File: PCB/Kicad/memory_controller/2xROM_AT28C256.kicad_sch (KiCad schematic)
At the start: 4 parts, among them U23 AT28C256-15PU, U24 AT28C256-15PU

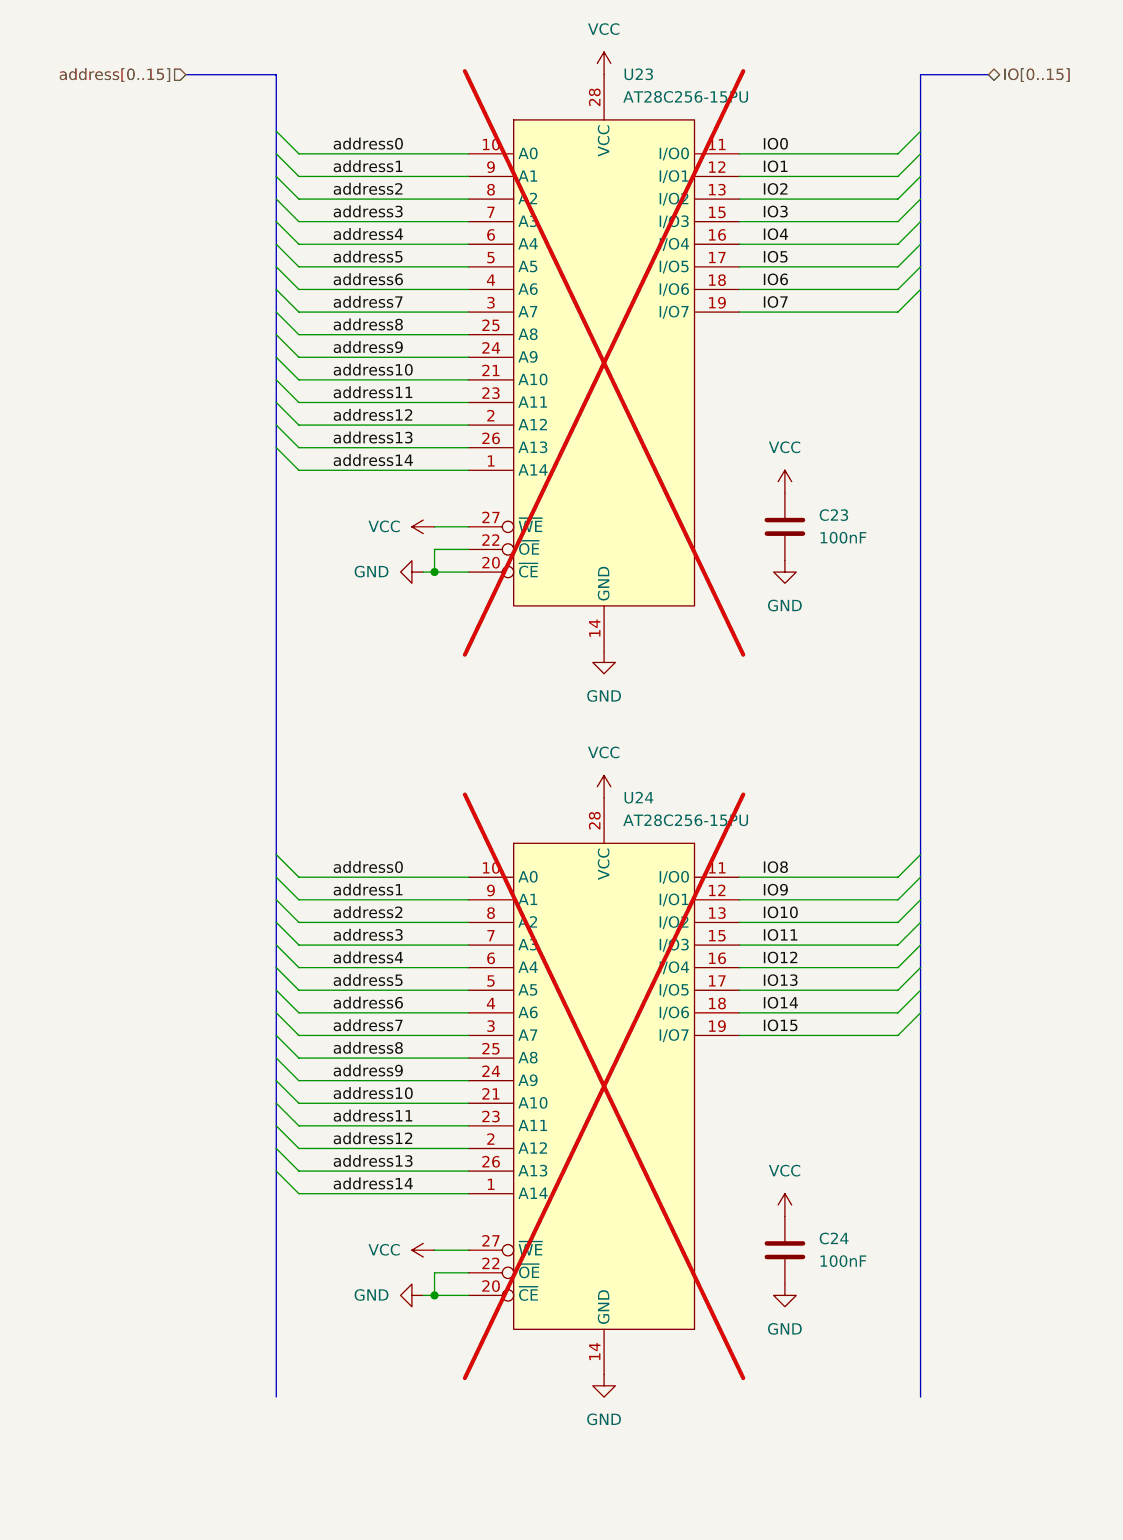
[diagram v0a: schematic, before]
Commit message: decoupling C RAM ROM
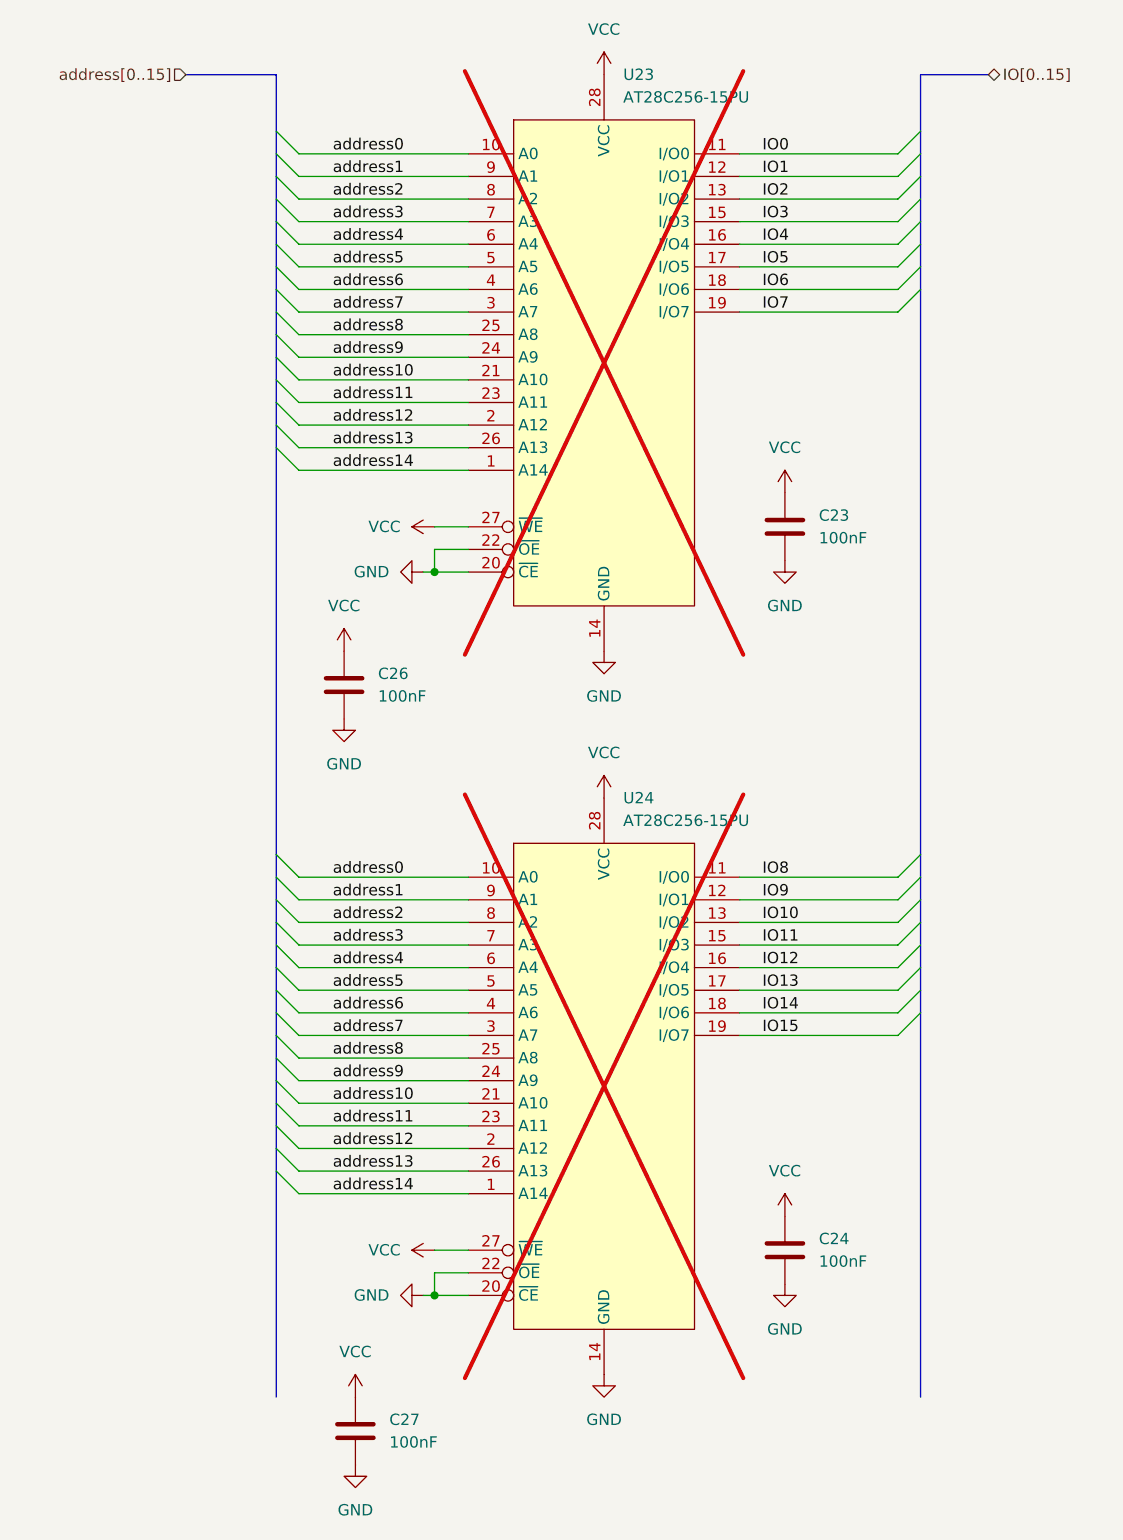
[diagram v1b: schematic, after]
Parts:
- added C26, C27: 100nF, Capacitor_SMD:C_0402_1005Metric, symbol Device:C
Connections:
- net GND: now also C26.1, C27.1
- net VCC: now also C26.2, C27.2

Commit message: board size + ground vias
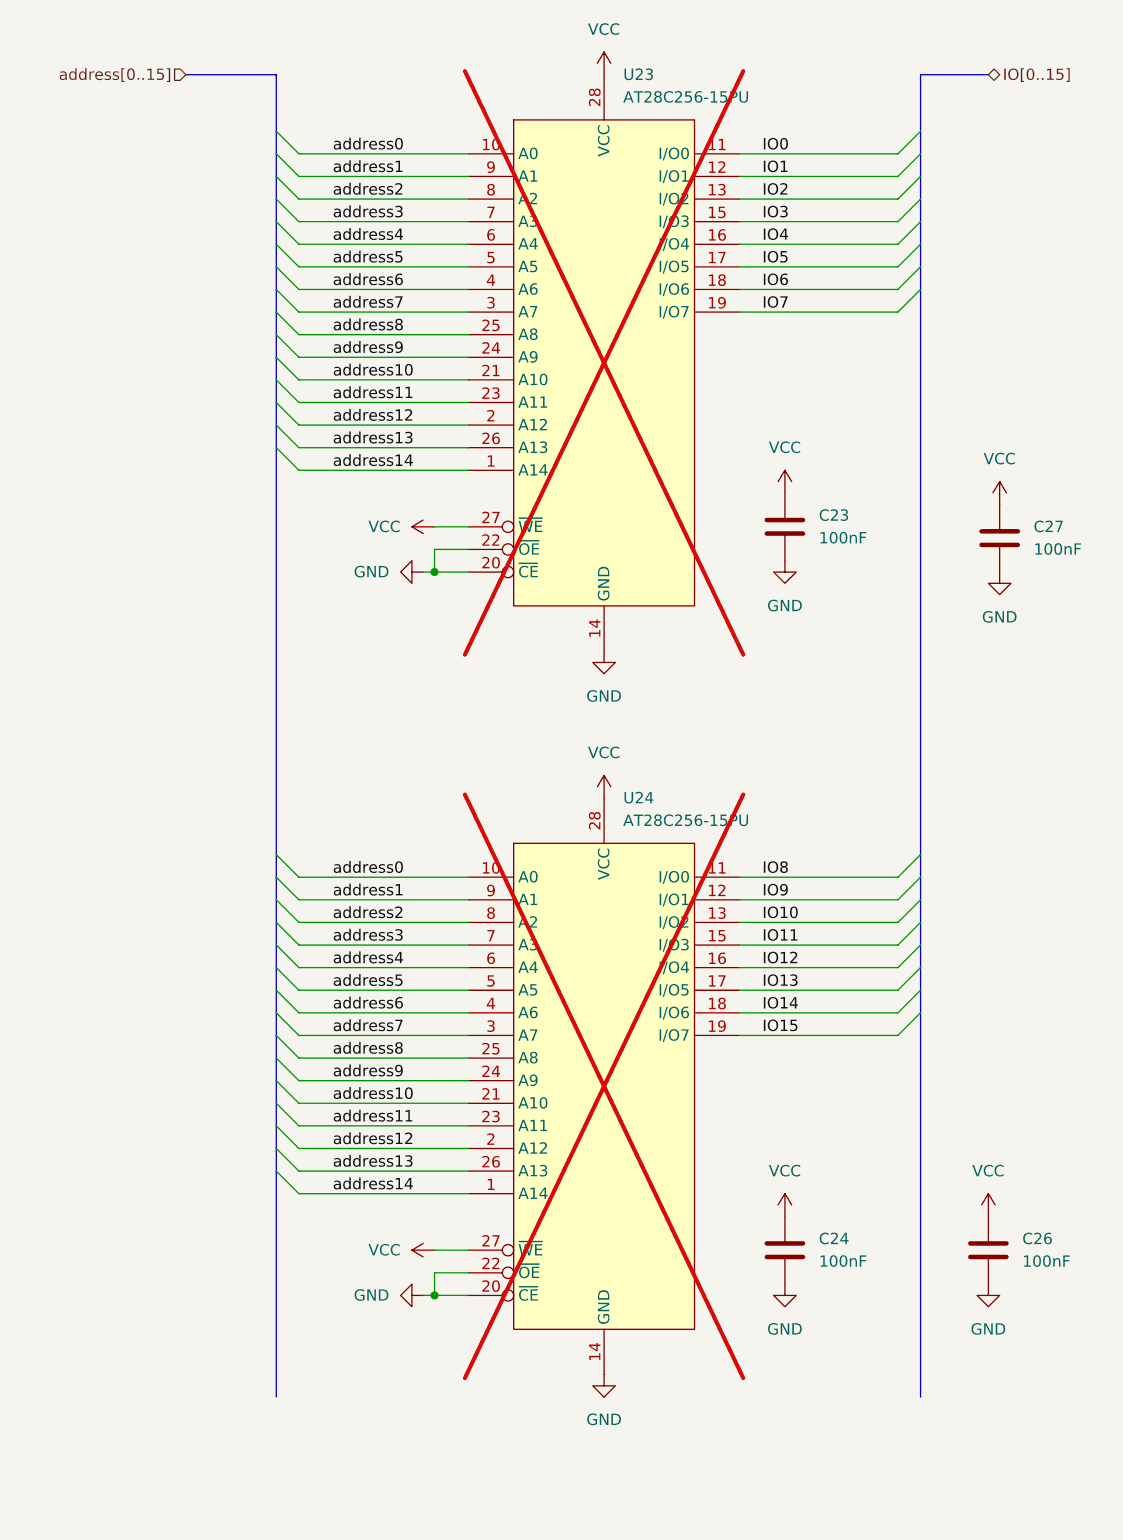
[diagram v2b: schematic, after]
